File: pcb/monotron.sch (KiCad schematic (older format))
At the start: 44 parts, among them J1 Mono / Stereo, J10 DIN5-180, J11 DIN5-180, J12 DE9M, J2 Jack-DC, J3 1x7 Header, J4 AudioJack3, J5 DE9F, J6 1x4 Header, J7 DE15HD, J8 2x6 Header, J9 DIN5-180, U1 TM4C123G_Launchpad, U2 MAX3232, U3 74LS14, U4 6N138

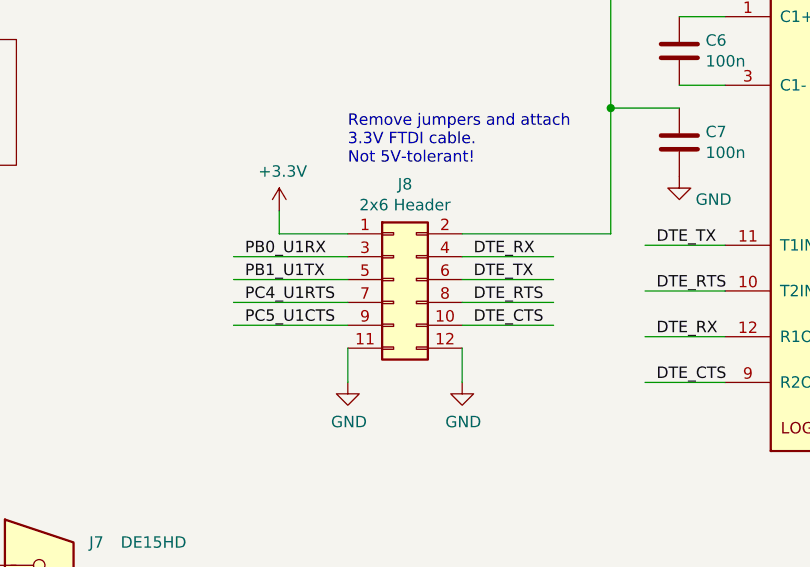
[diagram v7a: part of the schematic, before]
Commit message: Adjusted component layout again. ) More room between MIDI connectors. ) SD/MMC connector now under Launchpad board
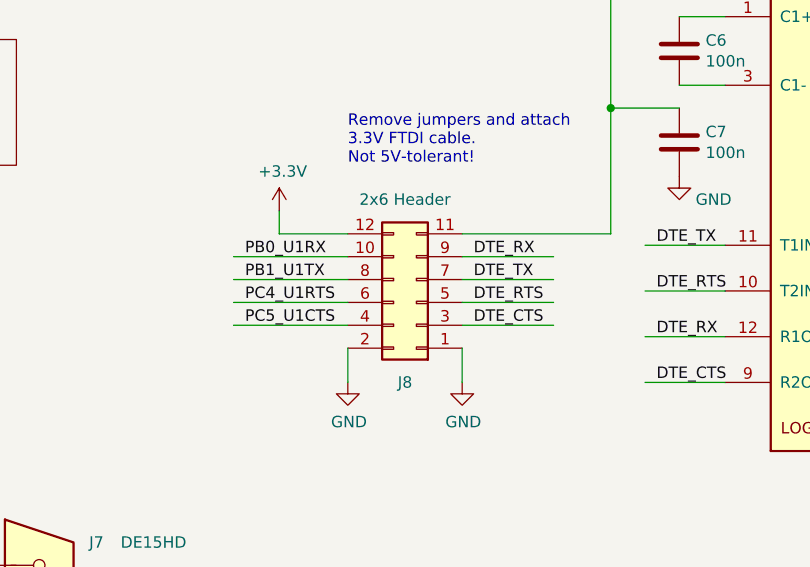
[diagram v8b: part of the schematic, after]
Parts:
- J10, J11, J9: footprint Launchpad:5P180 DIN Socket -> Monotron:5P180 DIN Socket
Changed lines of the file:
@@
 encoding utf-8
 Sheet 1 2
-Title "Monotron 32K"
-Date "2019-01-06"
+Title "Monotron 32K Schematic"
+Date "2019-01-10"
 Rev "0.1.0"
 Comp "https://github.com/thejpster/monotron"
-Comment1 "Copyright (c) Jonathan 'theJPster' Pallant 2018"
+Comment1 "Copyright (c) Jonathan 'theJPster' Pallant 2019"
 Comment2 "CC BY-SA 4.0"
 Comment3 ""
@@
 L Connector_Generic:Conn_02x06_Odd_Even J8
 U 1 1 5CE8C75D
-P 5900 4950
-F 0 "J8" H 5950 5367 50  0000 C CNN
-F 1 "2x6 Header" H 5950 5276 50  0000 C CNN
-F 2 "Connector_PinHeader_2.54mm:PinHeader_2x06_P2.54mm_Vertical" H 5900 4950 50  0001 C CNN
-F 3 "~" H 5900 4950 50  0001 C CNN
-F 4 "609-3263-ND‎" H 5900 4950 50  0001 C CNN "Digikey"
-	1    5900 4950
-	1    0    0    -1
+P 6000 5050
+F 0 "J8" H 6050 5400 50  0000 C CNN
+F 1 "2x6 Header" H 6050 4600 50  0000 C CNN
+F 2 "Connector_PinHeader_2.54mm:PinHeader_2x06_P2.54mm_Vertical" H 6000 5050 50  0001 C CNN
+F 3 "~" H 6000 5050 50  0001 C CNN
+F 4 "609-3263-ND‎" H 6000 5050 50  0001 C CNN "Digikey"
+	1    6000 5050
+	-1   0    0    1
 $EndComp
 $Comp
@@
 F 0 "J9" H 7850 826 50  0000 C CNN
 F 1 "DIN5-180" H 7850 735 50  0000 C CNN
-F 2 "Launchpad:5P180 DIN Socket" H 7850 1100 50  0001 C CNN
+F 2 "Monotron:5P180 DIN Socket" H 7850 1100 50  0001 C CNN
 F 3 "https://uk.rs-online.com/web/p/din-connectors/0491087/" H 7850 1100 50  0001 C CNN
 	1    7850 1100
@@
 F 0 "J11" H 9100 1500 50  0000 C CNN
 F 1 "DIN5-180" H 9100 1385 50  0000 C CNN
-F 2 "Launchpad:5P180 DIN Socket" H 9100 1750 50  0001 C CNN
+F 2 "Monotron:5P180 DIN Socket" H 9100 1750 50  0001 C CNN
 F 3 "https://uk.rs-online.com/web/p/din-connectors/0491087/" H 9100 1750 50  0001 C CNN
 	1    9100 1750
@@
 F 0 "J10" H 7850 2626 50  0000 C CNN
 F 1 "DIN5-180" H 7850 2535 50  0000 C CNN
-F 2 "Launchpad:5P180 DIN Socket" H 7850 2900 50  0001 C CNN
+F 2 "Monotron:5P180 DIN Socket" H 7850 2900 50  0001 C CNN
 F 3 "https://uk.rs-online.com/web/p/din-connectors/0491087/" H 7850 2900 50  0001 C CNN
 	1    7850 2900
